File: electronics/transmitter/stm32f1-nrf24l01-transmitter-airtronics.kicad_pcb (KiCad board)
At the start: 2 copper layers, 86.4 x 33 mm, 36 parts, among them K1 CONN_3, K10 CONN_3, K11 CONN_3, K12 UART, K2 CONN_3, K3 CONN_3, K4 CONN_3, K5 CONN_3, K6 CONN_3, K7 CONN_3, K8 CONN_3, K9 CONN_3, P1 Charge, P2 LED, P3 PWR-BAT, P4 PWR-IN, P5 Buzzer, P6 Meter, Q1 BC547B, SW1 ON/OFF, U1 LIPO_CHARGER_+_PROTECTION, U2 STM32F103C8T6_DEV_BOARD, U3 NRF24L01P

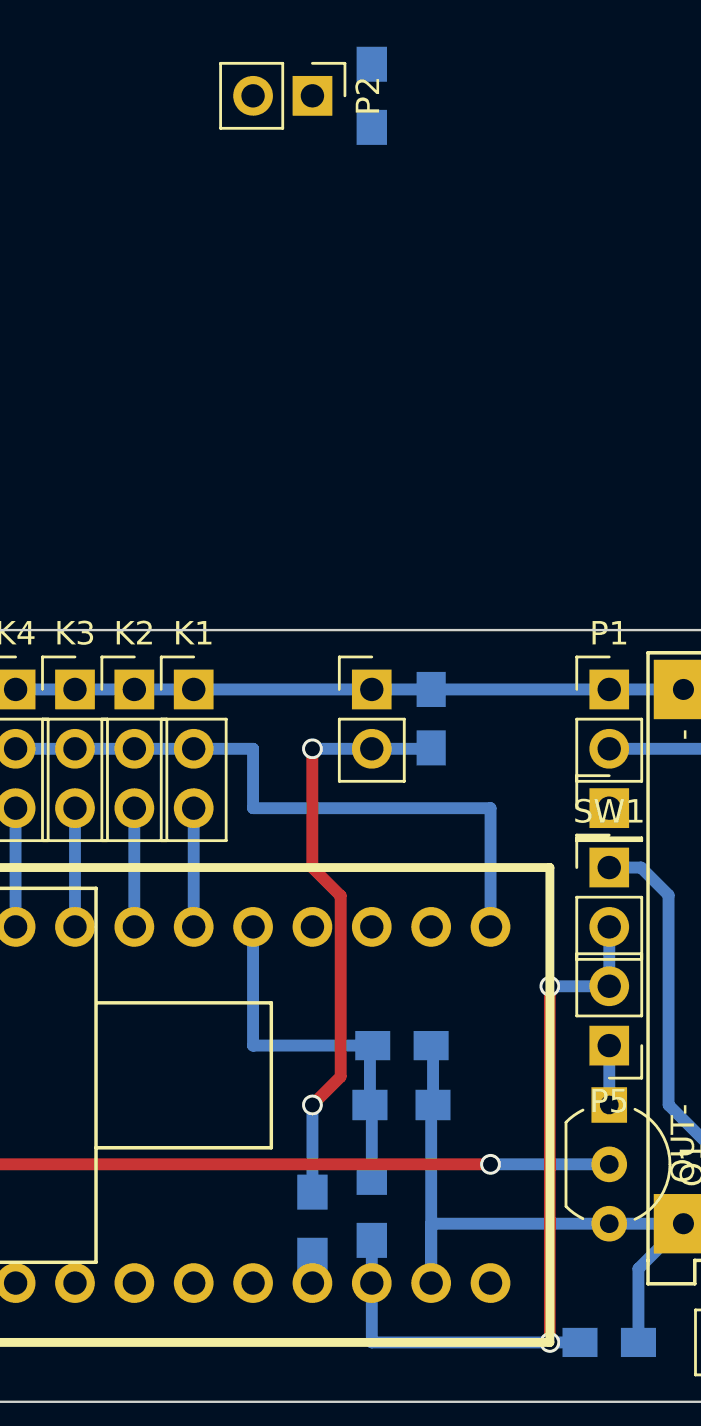
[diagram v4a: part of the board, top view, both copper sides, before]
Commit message: Tweak Airtronics PCB design
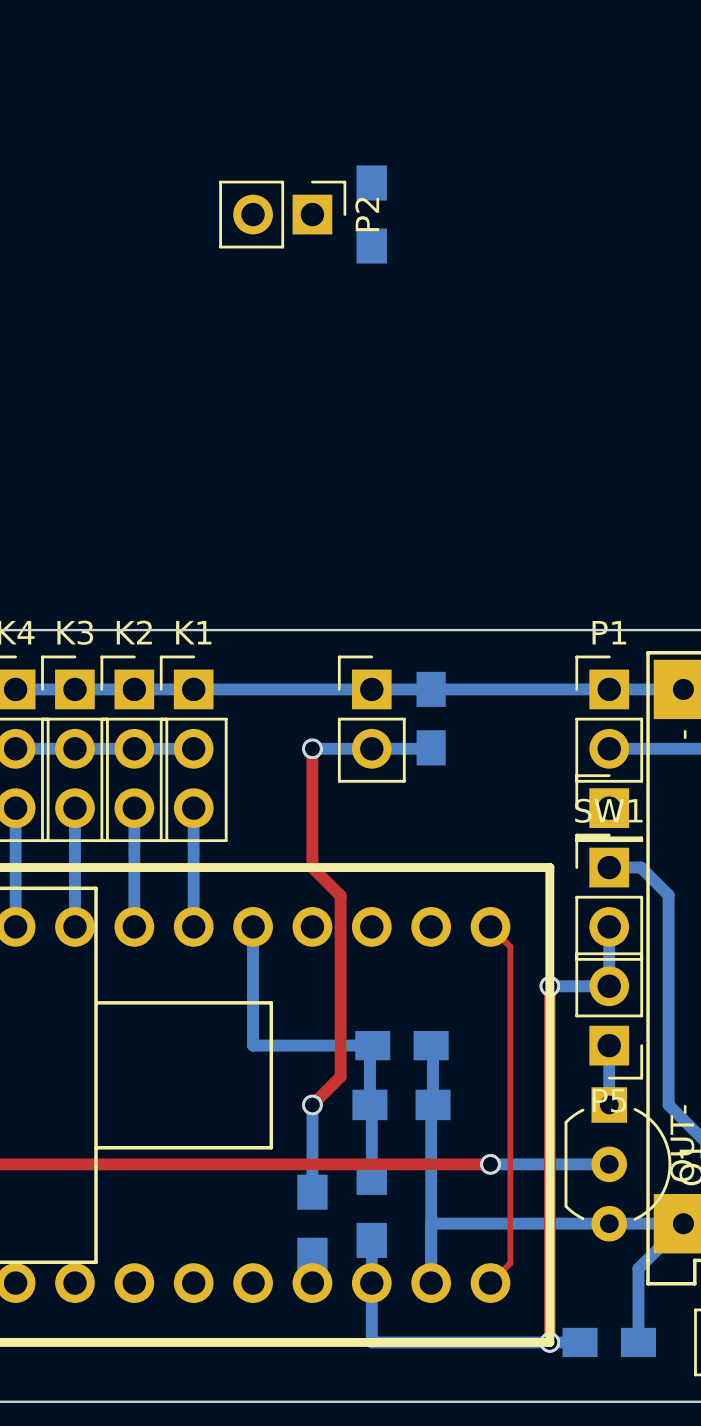
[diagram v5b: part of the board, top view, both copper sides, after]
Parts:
- moved P2 5.08 mm to (264.2, 88.9)
- moved R1 5.08 mm to (266.7, 88.9)
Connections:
- U2 pad 20: Net-(U2-Pad20) -> VCC
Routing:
- net VCC: track 74.7 -> 70.3 mm
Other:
- board text added: "CE to Vcc and cap on nRF board!"
- board text added: "Component modifications: STM32: remove BOOT pin header and tie to ground STM32: connect pin 20 and 21 with jumper on underside of PCB (instead of thin red trace shown!) STM32: change programming pin header to vertical style STM32: only add pin headers where needed (e.g. NOT Pin24) TP4056: Change charge resistor to 2k7 (440mA) TP4056: Remove tabs near batt pads TP4056: Remove red LED, connect to p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"
- board text added: "On STM32 PCB underside!"
- board text added: "This is not a PCB, but meant to be build on a perf board with round pads. It fits in the battery area of the Airtronics car transmitter."
- board text removed: "This is not a PCB, but meant to be build on a prototyping board. It fits in the battery area of the Airtronics car transmitter. Modifications needed: STM32: remove BOOT pin header and tie to ground STM32: change programming pin header to vertical style STM32: only add pin headers where needed (e.g. NOT Pin24) TP4056: Change charge resistor to 2k7 (440mA) TP4056: Remove tabs near batt pads TP4056: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"

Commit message: Remove values on connectors, fix-up meter resistor
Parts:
- R5: value 1k -> 3k9
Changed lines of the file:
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@@
   (general
     (links 85)
-    (no_connects 32)
+    (no_connects 31)
     (area 206.441257 86.373399 377.728568 171.5376)
     (thickness 1.6)
@@
       (effects (font (size 1 1) (thickness 0.15)))
     )
-    (fp_text value CONN_3 (at 0 7.47) (layer F.Fab)
+    (fp_text value CONN_3 (at 0 7.47) (layer F.Fab) hide
       (effects (font (size 1 1) (thickness 0.15)))
     )
@@
       (effects (font (size 1 1) (thickness 0.15)))
     )
-    (fp_text value CONN_3 (at 0 7.47) (layer F.Fab)
+    (fp_text value CONN_3 (at 0 7.47) (layer F.Fab) hide
       (effects (font (size 1 1) (thickness 0.15)))
     )
@@
       (effects (font (size 1 1) (thickness 0.15)))
     )
-    (fp_text value CONN_3 (at 0 7.47) (layer F.Fab)
+    (fp_text value CONN_3 (at 0 7.47) (layer F.Fab) hide
       (effects (font (size 1 1) (thickness 0.15)))
     )
@@
       (effects (font (size 1 1) (thickness 0.15)))
     )
-    (fp_text value CONN_3 (at 0 7.47) (layer F.Fab)
+    (fp_text value CONN_3 (at 0 7.47) (layer F.Fab) hide
       (effects (font (size 1 1) (thickness 0.15)))
     )
@@
       (effects (font (size 1 1) (thickness 0.15)))
     )
-    (fp_text value CONN_3 (at 0 7.47) (layer F.Fab)
+    (fp_text value CONN_3 (at 0 7.47) (layer F.Fab) hide
       (effects (font (size 1 1) (thickness 0.15)))
     )
@@
       (effects (font (size 1 1) (thickness 0.15)))
     )
-    (fp_text value CONN_3 (at 0 7.47) (layer F.Fab)
+    (fp_text value CONN_3 (at 0 7.47) (layer F.Fab) hide
       (effects (font (size 1 1) (thickness 0.15)))
     )
@@
       (effects (font (size 1 1) (thickness 0.15)))
     )
-    (fp_text value CONN_3 (at 0 7.47) (layer F.Fab)
+    (fp_text value CONN_3 (at 0 7.47) (layer F.Fab) hide
       (effects (font (size 1 1) (thickness 0.15)))
     )
@@
       (effects (font (size 1 1) (thickness 0.15)))
     )
-    (fp_text value CONN_3 (at 0 7.47) (layer F.Fab)
+    (fp_text value CONN_3 (at 0 7.47) (layer F.Fab) hide
       (effects (font (size 1 1) (thickness 0.15)))
     )
@@
       (effects (font (size 1 1) (thickness 0.15)))
     )
-    (fp_text value CONN_3 (at 0 7.47) (layer F.Fab)
+    (fp_text value CONN_3 (at 0 7.47) (layer F.Fab) hide
       (effects (font (size 1 1) (thickness 0.15)))
     )
@@
       (effects (font (size 1 1) (thickness 0.15)))
     )
-    (fp_text value CONN_3 (at 0 7.47) (layer F.Fab)
+    (fp_text value CONN_3 (at 0 7.47) (layer F.Fab) hide
       (effects (font (size 1 1) (thickness 0.15)))
     )
@@
       (effects (font (size 1 1) (thickness 0.15)))
     )
-    (fp_text value CONN_3 (at 0 7.47) (layer F.Fab)
+    (fp_text value CONN_3 (at 0 7.47) (layer F.Fab) hide
       (effects (font (size 1 1) (thickness 0.15)))
     )
@@
       (effects (font (size 1 1) (thickness 0.15)))
     )
-    (fp_text value Charge (at 0 4.93) (layer F.Fab)
+    (fp_text value Charge (at 0 4.93) (layer F.Fab) hide
       (effects (font (size 1 1) (thickness 0.15)))
     )
@@
       (effects (font (size 1 1) (thickness 0.15)))
     )
-    (fp_text value Buzzer (at 0 4.93 180) (layer F.Fab)
+    (fp_text value Buzzer (at 0 4.93 180) (layer F.Fab) hide
       (effects (font (size 1 1) (thickness 0.15)))
     )
@@
       (effects (font (size 1 1) (thickness 0.15)))
     )
-    (fp_text value MountingHole_3.2mm_M3 (at 0 4.2) (layer F.Fab)
+    (fp_text value MountingHole_3.2mm_M3 (at 0 4.2) (layer F.Fab) hide
       (effects (font (size 1 1) (thickness 0.15)))
     )
@@
       (effects (font (size 1 1) (thickness 0.15)))
     )
-    (fp_text value BATTERY (at 0 4.93 270) (layer F.Fab)
+    (fp_text value BATTERY (at 0 4.93 270) (layer F.Fab) hide
       (effects (font (size 1 1) (thickness 0.15)))
     )
@@
       (effects (font (size 1 1) (thickness 0.15)))
     )
-    (fp_text value Meter (at 0 4.93) (layer F.Fab)
+    (fp_text value Meter (at 0 4.93) (layer F.Fab) hide
       (effects (font (size 1 1) (thickness 0.15)))
     )
@@
       (effects (font (size 1 1) (thickness 0.15)) (justify mirror))
     )
-    (fp_text value 1k (at 0 -1.75 90) (layer Eco2.User)
+    (fp_text value 3k9 (at 0 -1.75 90) (layer Eco2.User)
       (effects (font (size 1 1) (thickness 0.15)))
     )
@@
       (effects (font (size 1 1) (thickness 0.15)))
     )
-    (fp_text value ON/OFF (at 0 4.93) (layer F.Fab)
+    (fp_text value ON/OFF (at 0 4.93) (layer F.Fab) hide
       (effects (font (size 1 1) (thickness 0.15)))
     )
@@
       (effects (font (size 1 1) (thickness 0.15)))
     )
-    (fp_text value Pin_Header_Straight_1x01_Pitch2.54mm (at 0 2.39) (layer F.Fab)
-      (effects (font (size 1 1) (thickness 0.15)))
-    )
+    (fp_text value Pin_Header_Straight_1x01_Pitch2.54mm (at 0 2.39) (layer F.Fab) hide
+      (effects (font (size 1 1) (thickness 0.15)))
+    )
